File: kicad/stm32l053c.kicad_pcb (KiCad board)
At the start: 2 copper layers, 26.7 x 43.2 mm, 45 parts, among them J1 GND, J10 3V3, J11 I2C, J2 GND, J3 TX, J4 GND, J5 TEST_1P, J6 TEST_1P, J8 RX, P1 SWD, U1 AP2112, U2 STM32L053C8_LQFP48, U3 ADS1015, U4 UFL_SMA, U5 RFM92/95

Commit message: Start of layout
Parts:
- removed A0: A0, Pin_Headers:Pin_Header_Straight_1x01_Pitch2.54mm
- removed A1: A1, Pin_Headers:Pin_Header_Straight_1x01_Pitch2.54mm
- removed A2: A2, Pin_Headers:Pin_Header_Straight_1x01_Pitch2.54mm
- removed BT1: Battery, theapi:BatteryBoxAndPins
- removed C4: 10uF, Capacitors_SMD:C_0805_HandSoldering
- removed J10: 3V3, Pin_Headers:Pin_Header_Straight_1x01_Pitch2.54mm
- removed J11: I2C, Pin_Headers:Pin_Header_Straight_1x04_Pitch2.54mm
- removed J8: RX, Pin_Headers:Pin_Header_Straight_1x01_Pitch2.54mm
- removed PA6: A3, Pin_Headers:Pin_Header_Straight_1x01_Pitch2.54mm
- removed REF**: TheApiLogoTiny, theapi:TheApiLogoTiny
- removed REF**: TheApiLogo, theapi:TheApiLogoSmall
- removed SC1: Solar_Cells, Pin_Headers:Pin_Header_Straight_1x02_Pitch2.54mm
- added H1: MountingHole_Pad, MountingHole:MountingHole_3.2mm_M3_Pad, F.Cu at (83.8, 55.9)
- added H2: MountingHole_Pad, MountingHole:MountingHole_3.2mm_M3_Pad, F.Cu at (83.8, 104.1)
- added H3: MountingHole_Pad, MountingHole:MountingHole_3.2mm_M3_Pad, F.Cu at (166.4, 55.9)
- added H4: MountingHole_Pad, MountingHole:MountingHole_3.2mm_M3_Pad, F.Cu at (166.4, 104.1)
- added J7: BATTERY, Connector_JST:JST_XH_B02B-XH-A_1x02_P2.50mm_Vertical, F.Cu at (104.1, 101.6)
- added Q1: Q_NMOS_GSD, Package_TO_SOT_SMD:SOT-23_Handsoldering, F.Cu at (184.3, 53.3)
- added R12: 100K, Resistor_SMD:R_0805_2012Metric_Pad1.15x1.40mm_HandSolder, F.Cu at (175.0, 59.3)
- added R13: 1K, Resistor_SMD:R_0603_1608Metric_Pad1.05x0.95mm_HandSolder, F.Cu at (187.0, 55.8)
- added R14: 620K, Resistor_SMD:R_0805_2012Metric_Pad1.15x1.40mm_HandSolder, F.Cu at (200.5, 51.4)
- added R15: 100K, Resistor_SMD:R_0805_2012Metric_Pad1.15x1.40mm_HandSolder, F.Cu at (200.5, 53.4)
- added R16: 820, Resistor_SMD:R_0805_2012Metric_Pad1.15x1.40mm_HandSolder, F.Cu at (183.4, 56.0)
- added R17: 820, Resistor_SMD:R_0805_2012Metric_Pad1.15x1.40mm_HandSolder, F.Cu at (178.7, 59.3)
- added R18: 820, Resistor_SMD:R_0805_2012Metric_Pad1.15x1.40mm_HandSolder, F.Cu at (183.4, 58.0)
- added TH1: Thermistor_NTC, Connector_JST:JST_XH_B02B-XH-A_1x02_P2.50mm_Vertical, F.Cu at (104.1, 71.1)
- D2: value D_Schottky -> LED_CRGB; footprint theapi:D_SOD-323_HandSoldering -> Connector_JST:JST_XH_B04B-XH-A_1x04_P2.50mm_Vertical; moved to F.Cu
- J1: value GND -> Water_Level; footprint Pin_Headers:Pin_Header_Straight_1x01_Pitch2.54mm -> Connector_JST:JST_XH_B02B-XH-A_1x02_P2.50mm_Vertical
- J2: value GND -> Motion; footprint Pin_Headers:Pin_Header_Straight_1x01_Pitch2.54mm -> Connector_JST:JST_XH_B03B-XH-A_1x03_P2.50mm_Vertical
- J3: value TX -> Door; footprint Pin_Headers:Pin_Header_Straight_1x01_Pitch2.54mm -> Connector_JST:JST_XH_B02B-XH-A_1x02_P2.50mm_Vertical
- J4: value GND -> Door_Led; footprint Pin_Headers:Pin_Header_Straight_1x01_Pitch2.54mm -> Connector_JST:JST_XH_B02B-XH-A_1x02_P2.50mm_Vertical
- J5: value TEST_1P -> AIN3; footprint theapi:TestPoint -> Connector_PinHeader_2.54mm:PinHeader_1x02_P2.54mm_Vertical
- J6: value TEST_1P -> Pump; footprint theapi:TestPoint -> Connector_PinHeader_2.54mm:PinHeader_1x01_P2.54mm_Vertical
- R1, R7, R9: footprint Resistors_SMD:R_0805_HandSoldering -> Resistor_SMD:R_0805_2012Metric_Pad1.15x1.40mm_HandSolder
- R10, R2, R3, R4: footprint Resistors_SMD:R_0805_HandSoldering -> Resistor_SMD:R_0603_1608Metric_Pad1.05x0.95mm_HandSolder
- R11: value 4K7 -> 100K; footprint Resistors_SMD:R_0805_HandSoldering -> Resistor_SMD:R_0805_2012Metric_Pad1.15x1.40mm_HandSolder
- R5: value R_Shunt -> 0.01R; footprint theapi:SHUNT_1210_HandSoldering -> Connector_JST:JST_XH_B02B-XH-A_1x02_P2.50mm_Vertical; moved to F.Cu
- R6: value 300K -> 10K; footprint Resistors_SMD:R_0805_HandSoldering -> Resistor_SMD:R_0603_1608Metric_Pad1.05x0.95mm_HandSolder
- R8: value 100K -> 620K; footprint Resistors_SMD:R_0805_HandSoldering -> Resistor_SMD:R_0805_2012Metric_Pad1.15x1.40mm_HandSolder
- U1: value AP2112 -> MCP1703A-3302_SOT223; footprint TO_SOT_Packages_SMD:SOT-23-5_HandSoldering -> Package_TO_SOT_SMD:SOT-223-3_TabPin2; moved to F.Cu
- U3: footprint Housings_SSOP:TSSOP-10_3x3mm_Pitch0.5mm -> Package_SO:TSSOP-10_3x3mm_P0.5mm
- moved J4 77.5 mm to (83.8, 86.4), turned to 0 degrees
- moved J1 65.9 mm to (83.8, 71.1)
- moved J3 60.6 mm to (104.1, 86.4)
- moved D2 56.7 mm to (91.4, 55.9), turned to 0 degrees
- moved J2 44.4 mm to (116.8, 55.9)
- moved U1 18.5 mm to (124.5, 94.0), turned to 90 degrees
- moved R5 16.9 mm to (124.5, 71.1), turned to 0 degrees
- moved J5 9.78 mm to (165.1, 78.7)
- moved J6 3.94 mm to (160.0, 86.4)
- moved C8 1.63 mm to (138.2, 62.5)
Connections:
- net PA2 renamed USART2_TX
- C5 pad 1: /BATT -> +BATT
- D2 pad 1: /BATT -> Earth
- D2 pad 2: Net-(D2-Pad2) -> (no net)
- J1 pad 1: Earth -> SENSOR_PWR
- J2 pad 1: Earth -> +3V3
- J3 pad 1: USART1_TX -> +3V3
- J4 pad 1: Earth -> +3V3
- J5 pad 1: /PA4 -> Earth
- J6 pad 1: /PA3 -> PUMP
- R11 pad 1: +3V3 -> MOTION
- R11 pad 2: /1_WIRE -> Earth
- R5 pad 1: Net-(R5-Pad1) -> /AIN0
- R5 pad 2: /AIN0 -> /AIN1
- R6 pad 1: Net-(D2-Pad2) -> SENSOR_PWR
- R6 pad 2: /AIN2 -> WATER_TEMP
- R7 pad 1: /AIN2 -> WATER_LEVEL
- R8 pad 1: /BATT -> +BATT
- R8 pad 2: /AIN3 -> /AIN2
- R9 pad 1: /AIN3 -> /AIN2
- U1 pad 1: /BATT -> +BATT
- U1 pad 3: /BATT -> +3V3
- U2 pad 10: Net-(U2-Pad10) -> WATER_TEMP
- U2 pad 11: Net-(U2-Pad11) -> WATER_LEVEL
- U2 pad 13: /PA3 -> (no net)
- U2 pad 14: /PA4 -> SENSOR_PWR
- U2 pad 16: /1_WIRE -> DOOR_LED
- U2 pad 17: Net-(A2-Pad1) -> (no net)
- U2 pad 18: Net-(A1-Pad1) -> LED_RED
- U2 pad 19: Net-(A0-Pad1) -> LED_GREEN
- U2 pad 2: Net-(U2-Pad2) -> PUMP
- U2 pad 20: Net-(U2-Pad20) -> LED_BLUE
- U2 pad 21: DIO5 -> DIO0
- U2 pad 29: Net-(U2-Pad29) -> (no net)
- U2 pad 3: Net-(U2-Pad3) -> (no net)
- U2 pad 30: USART1_TX -> (no net)
- U2 pad 31: USART1_RX -> (no net)
- U2 pad 32: Net-(U2-Pad32) -> MOTION
- U2 pad 33: Net-(U2-Pad33) -> DOOR
- U2 pad 38: DIO3 -> (no net)
- U2 pad 39: DIO4 -> (no net)
- U2 pad 4: Net-(U2-Pad4) -> (no net)
- U2 pad 40: DIO0 -> (no net)
- U2 pad 41: DIO1 -> ADC_RDY
- U2 pad 45: DIO2 -> (no net)
- U2 pad 46: ADC_RDY -> (no net)
- U2 pad 5: Net-(U2-Pad5) -> (no net)
- U2 pad 6: Net-(U2-Pad6) -> (no net)
- U5 pad 11: DIO3 -> (no net)
- U5 pad 12: DIO4 -> (no net)
- U5 pad 15: DIO1 -> (no net)
- U5 pad 16: DIO2 -> (no net)
- U5 pad 7: DIO5 -> (no net)
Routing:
- net +3V3: track 172.7 -> 77.6 mm, vias 5 -> 4
- net Earth: track 210.2 -> 118.7 mm, vias 8 -> 6
- net /BATT: track 54.0 -> 0.00 mm, vias 1 -> 0
- net Net-(D2-Pad2): track 27.4 -> 0.00 mm
- net DIO5: track 26.8 -> 0.00 mm
- net USART1_RX: track 23.4 -> 0.00 mm, vias 1 -> 0
- net USART1_TX: track 23.4 -> 0.00 mm, vias 1 -> 0
- net +BATT: track 0.00 -> 20.9 mm, vias 0 -> 1
- net DIO3: track 19.4 -> 0.00 mm
- net DIO4: track 18.0 -> 0.00 mm
- net I2C1_SCL: track 32.6 -> 15.2 mm
- net /AIN0: track 15.4 -> 0.00 mm
- net I2C1_SDA: track 33.6 -> 18.5 mm
- net DIO0: track 15.5 -> 1.45 mm
- net DIO1: track 13.2 -> 0.00 mm
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- removed copper zone on B.Cu, net Earth
- removed copper zone on F.Cu, net Earth
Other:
- board size 26.7 x 43.2 mm -> 90 x 55 mm
- board text added: "BAT+"
- board text added: "BAT-"
- board text removed: "+"
- board text removed: "-"
- board text removed: "1WIRE"
- board text removed: "A0"
- board text removed: "A1"
- board text removed: "A2"
- board text removed: "BAT"
- board text removed: "SCL"
- board text removed: "SDA"
- board text removed: "SOL"

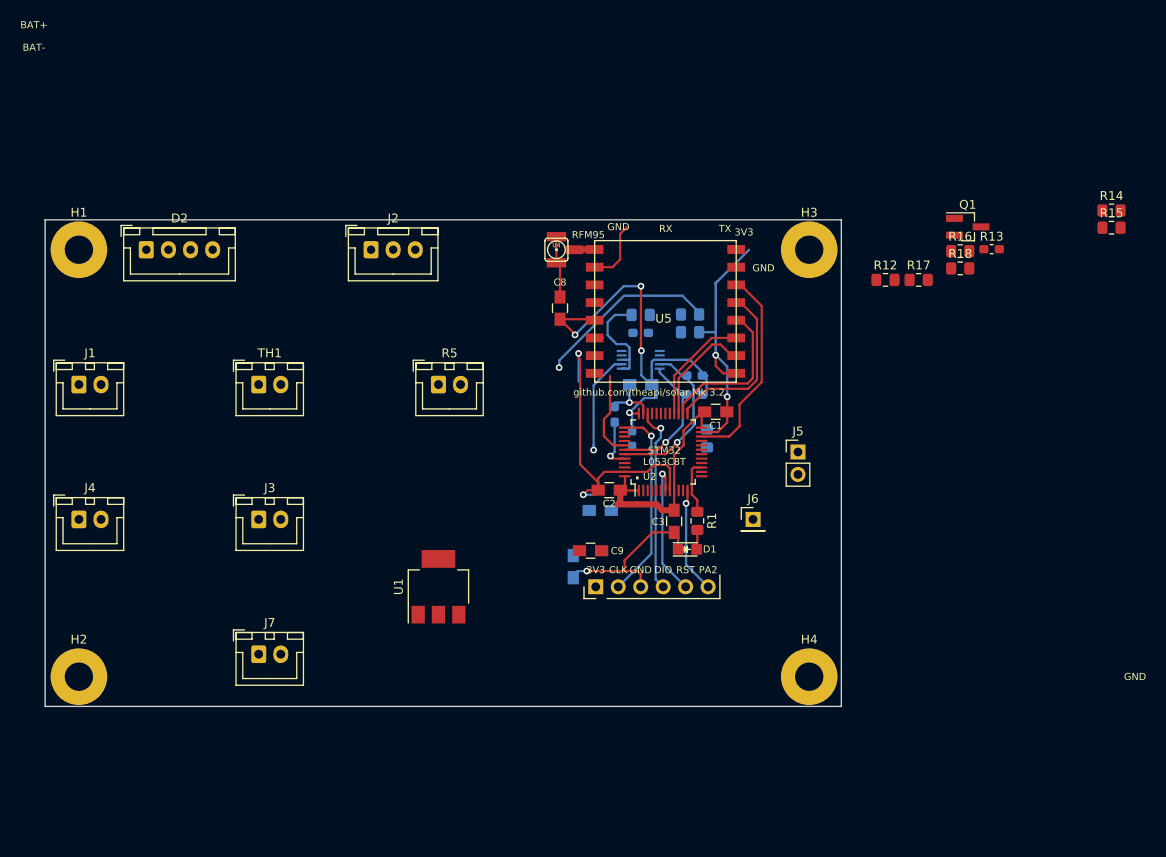
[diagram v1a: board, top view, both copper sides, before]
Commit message: Two voltage regulator layout
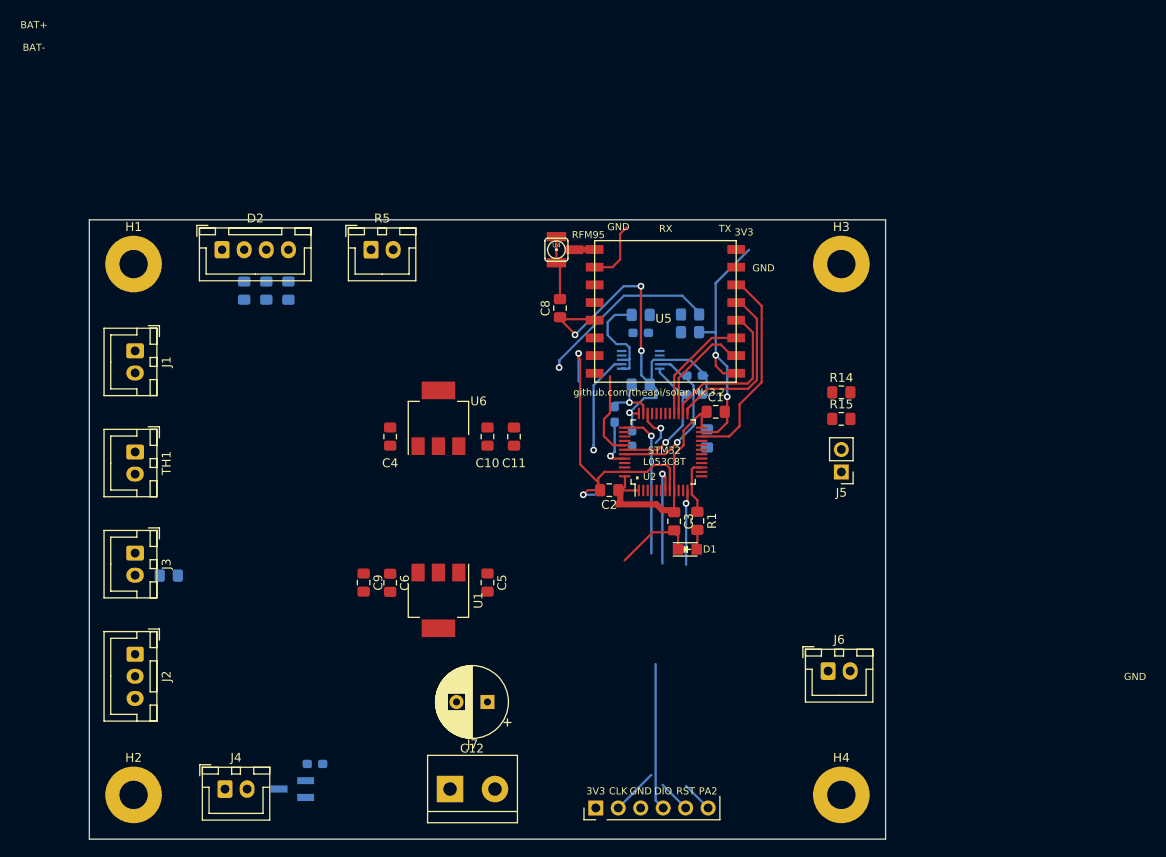
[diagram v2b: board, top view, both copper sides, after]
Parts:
- added C10: 1uf, Capacitor_SMD:C_0805_2012Metric_Pad1.15x1.40mm_HandSolder, F.Cu at (130.0, 77.0)
- added C11: 10uF, Capacitor_SMD:C_0805_2012Metric_Pad1.15x1.40mm_HandSolder, F.Cu at (133.0, 77.0)
- added C12: CP, Capacitor_THT:CP_Radial_D8.0mm_P3.50mm, F.Cu at (130.0, 107.0)
- added C4: 1uf, Capacitor_SMD:C_0805_2012Metric_Pad1.15x1.40mm_HandSolder, F.Cu at (119.0, 77.0)
- added U6: MCP1703A-3302_SOT223, Package_TO_SOT_SMD:SOT-223-3_TabPin2, F.Cu at (124.5, 74.9)
- C1, C2, C3, C7, C8, C9: footprint Capacitors_SMD:C_0805_HandSoldering -> Capacitor_SMD:C_0805_2012Metric_Pad1.15x1.40mm_HandSolder
- C5, C6: footprint Capacitors_SMD:C_0805_HandSoldering -> Capacitor_SMD:C_0805_2012Metric_Pad1.15x1.40mm_HandSolder; moved to F.Cu
- J6: footprint Connector_PinHeader_2.54mm:PinHeader_1x01_P2.54mm_Vertical -> Connector_JST:JST_XH_B02B-XH-A_1x02_P2.50mm_Vertical
- J7: footprint Connector_JST:JST_XH_B02B-XH-A_1x02_P2.50mm_Vertical -> TerminalBlock:TerminalBlock_bornier-2_P5.08mm
- Q1, R12, R13, R16, R17, R18: moved to B.Cu
- U1: value MCP1703A-3302_SOT223 -> MCP1703A-5002_SOT223
- moved Q1 99.3 mm to (108.0, 116.8), turned to 180 degrees
- moved R13 96.1 mm to (110.5, 114.0), turned to 180 degrees
- moved R12 87.6 mm to (94.0, 92.7)
- moved R16 81.1 mm to (102.5, 60.5), turned to 90 degrees
- moved R18 76.0 mm to (107.5, 60.5), turned to 90 degrees
- moved R17 73.7 mm to (105.0, 60.5), turned to 90 degrees
- moved J2 52.9 mm to (90.2, 101.6), turned to 270 degrees
- moved R15 37.4 mm to (170.0, 75.0)
- moved R14 36.8 mm to (170.0, 72.0)
- moved J4 34.7 mm to (100.3, 116.8)
- moved J7 26.5 mm to (125.8, 116.8)
- moved C9 25.9 mm to (116.0, 93.5), turned to 270 degrees
- moved P1 25.0 mm to (142.2, 119.0)
- moved C6 20.8 mm to (119.0, 93.5)
- moved J6 19.1 mm to (168.5, 103.5)
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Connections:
- C6 pad 1: +3V3 -> +5V
- C9 pad 1: +3V3 -> +5V
- D2 pad 2: (no net) -> Net-(D2-Pad2)
- D2 pad 3: (no net) -> Net-(D2-Pad3)
- D2 pad 4: (no net) -> Net-(D2-Pad4)
- J2 pad 1: +3V3 -> +5V
- J4 pad 1: +3V3 -> +5V
- J7 pad 1: +BATT -> Earth
- J7 pad 2: Earth -> +BATT
- R16 pad 2: (no net) -> Net-(D2-Pad2)
- R17 pad 2: (no net) -> Net-(D2-Pad3)
- R18 pad 2: (no net) -> Net-(D2-Pad4)
- U1 pad 3: +3V3 -> +5V
- U2 pad 13: (no net) -> USART2_RX
- U2 pad 17: (no net) -> Net-(U2-Pad17)
- U2 pad 29: (no net) -> Net-(U2-Pad29)
- U2 pad 3: (no net) -> Net-(U2-Pad3)
- U2 pad 30: (no net) -> Net-(U2-Pad30)
- U2 pad 31: (no net) -> Net-(U2-Pad31)
- U2 pad 38: (no net) -> Net-(U2-Pad38)
- U2 pad 39: (no net) -> Net-(U2-Pad39)
- U2 pad 4: (no net) -> Net-(U2-Pad4)
- U2 pad 40: (no net) -> Net-(U2-Pad40)
- U2 pad 45: (no net) -> Net-(U2-Pad45)
- U2 pad 46: (no net) -> Net-(U2-Pad46)
- U2 pad 5: (no net) -> Net-(U2-Pad5)
- U2 pad 6: (no net) -> Net-(U2-Pad6)
- U5 pad 11: (no net) -> Net-(U5-Pad11)
- U5 pad 12: (no net) -> Net-(U5-Pad12)
- U5 pad 15: (no net) -> Net-(U5-Pad15)
- U5 pad 16: (no net) -> Net-(U5-Pad16)
- U5 pad 7: (no net) -> Net-(U5-Pad7)
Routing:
- net Earth: track 118.7 -> 108.1 mm, vias 6 -> 5
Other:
- board size 90 x 55 mm -> 90 x 70 mm

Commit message: Protection
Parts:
- added D3: 3V6, Diode_THT:D_T-1_P5.08mm_Horizontal, F.Cu at (130.0, 83.6)
- added F1: Polyfuse, Resistor_SMD:R_1812_4532Metric_Pad1.30x3.40mm_HandSolder, F.Cu at (130.8, 104.0)
- added Q2: Q_PMOS_GSD, Package_TO_SOT_SMD:SOT-23_Handsoldering, F.Cu at (129.8, 109.6)
- added R19: 1K, Resistor_SMD:R_0603_1608Metric_Pad1.05x0.95mm_HandSolder, B.Cu at (119.2, 60.2)
- added R20: 1K, Resistor_SMD:R_0603_1608Metric_Pad1.05x0.95mm_HandSolder, B.Cu at (116.8, 60.2)
- added R21: 1K, Resistor_SMD:R_0603_1608Metric_Pad1.05x0.95mm_HandSolder, F.Cu at (136.0, 77.0)
- moved C12 8.81 mm to (121.2, 106.6)
- moved J7 2.77 mm to (123.0, 116.8)
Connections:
- C12 pad 1: +BATT -> Net-(C12-Pad1)
- C12 pad 2: Earth -> Net-(C12-Pad2)
- C5 pad 1: +BATT -> Net-(C12-Pad1)
- C5 pad 2: Earth -> Net-(C12-Pad2)
- R5 pad 1: /AIN0 -> Net-(R20-Pad2)
- R5 pad 2: /AIN1 -> Net-(R19-Pad2)
- R8 pad 1: +BATT -> /BATT
- U1 pad 1: +BATT -> Net-(C12-Pad1)
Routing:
- net SWDIO: track 21.2 -> 46.5 mm
- net NRST: track 15.8 -> 40.8 mm
- net USART2_TX: track 12.0 -> 37.0 mm
- net SWCLK: track 22.0 -> 47.0 mm
- net /BATT: track 0.00 -> 20.9 mm, vias 0 -> 1
- net +BATT: track 20.9 -> 0.00 mm, vias 1 -> 0
- net Earth: track 108.1 -> 90.0 mm
- net ADC_RDY: track 21.3 -> 13.2 mm
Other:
- board text added: "5V"

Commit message: Solder mask for the ADS1015
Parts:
- U3: footprint Package_SO:TSSOP-10_3x3mm_P0.5mm -> theapi:TSSOP-10_3x3mm_P0.5mm
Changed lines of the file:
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@@
-    )
-  )
-  (module Package_SO:TSSOP-10_3x3mm_P0.5mm (layer B.Cu)
-    (at 147.32 68.326)
-    (descr "TSSOP10: plastic thin shrink small outline package; 10 leads; body width 3 mm; (see NXP SSOP-TSSOP-VSO-REFLOW.pdf and sot552-1_po.pdf)")
-    (tags "SSOP 0.5")
-    (attr smd)
-    (fp_text reference U3 (at 0 2.55) (layer B.SilkS)
-      (effects (font (size 1 1) (thickness 0.15)) (justify mirror))
-    )
-    (fp_text value ADS1015 (at 0 -2.55) (layer B.Fab)
-      (effects (font (size 1 1) (thickness 0.15)) (justify mirror))
-    )
-    (fp_line (start -0.5 1.5) (end 1.5 1.5) (layer B.Fab) (width 0.15))
-    (fp_line (start 1.5 1.5) (end 1.5 -1.5) (layer B.Fab) (width 0.15))
-    (fp_line (start 1.5 -1.5) (end -1.5 -1.5) (layer B.Fab) (width 0.15))
-    (fp_line (start -1.5 -1.5) (end -1.5 0.5) (layer B.Fab) (width 0.15))
-    (fp_line (start -1.5 0.5) (end -0.5 1.5) (layer B.Fab) (width 0.15))
-    (fp_line (start -2.95 1.8) (end -2.95 -1.8) (layer B.CrtYd) (width 0.05))
-    (fp_line (start 2.95 1.8) (end 2.95 -1.8) (layer B.CrtYd) (width 0.05))
-    (fp_line (start -2.95 1.8) (end 2.95 1.8) (layer B.CrtYd) (width 0.05))
-    (fp_line (start -2.95 -1.8) (end 2.95 -1.8) (layer B.CrtYd) (width 0.05))
-    (fp_line (start -1.625 1.625) (end -1.625 1.45) (layer B.SilkS) (width 0.15))
-    (fp_line (start 1.625 1.625) (end 1.625 1.35) (layer B.SilkS) (width 0.15))
-    (fp_line (start 1.625 -1.625) (end 1.625 -1.35) (layer B.SilkS) (width 0.15))
-    (fp_line (start -1.625 -1.625) (end -1.625 -1.35) (layer B.SilkS) (width 0.15))
-    (fp_line (start -1.625 1.625) (end 1.625 1.625) (layer B.SilkS) (width 0.15))
-    (fp_line (start -1.625 -1.625) (end 1.625 -1.625) (layer B.SilkS) (width 0.15))
-    (fp_line (start -1.625 1.45) (end -2.7 1.45) (layer B.SilkS) (width 0.15))
-    (fp_text user %R (at 0 0) (layer B.Fab)
-      (effects (font (size 0.6 0.6) (thickness 0.15)) (justify mirror))
-    )
-    (pad 1 smd rect (at -2.15 1) (size 1.1 0.25) (layers B.Cu B.Paste B.Mask)
-      (net 1 Earth))
-    (pad 2 smd rect (at -2.15 0.5) (size 1.1 0.25) (layers B.Cu B.Paste B.Mask)
-      (net 9 ADC_RDY))
-    (pad 3 smd rect (at -2.15 0) (size 1.1 0.25) (layers B.Cu B.Paste B.Mask)
-      (net 1 Earth))
-    (pad 4 smd rect (at -2.15 -0.5) (size 1.1 0.25) (layers B.Cu B.Paste B.Mask)
-      (net 19 /AIN0))
-    (pad 5 smd rect (at -2.15 -1) (size 1.1 0.25) (layers B.Cu B.Paste B.Mask)
-      (net 21 /AIN1))
-    (pad 6 smd rect (at 2.15 -1) (size 1.1 0.25) (layers B.Cu B.Paste B.Mask)
-      (net 13 /AIN2))
-    (pad 7 smd rect (at 2.15 -0.5) (size 1.1 0.25) (layers B.Cu B.Paste B.Mask)
-      (net 20 /AIN3))
-    (pad 8 smd rect (at 2.15 0) (size 1.1 0.25) (layers B.Cu B.Paste B.Mask)
-      (net 6 +3V3))
-    (pad 9 smd rect (at 2.15 0.5) (size 1.1 0.25) (layers B.Cu B.Paste B.Mask)
-      (net 7 I2C1_SDA))
-    (pad 10 smd rect (at 2.15 1) (size 1.1 0.25) (layers B.Cu B.Paste B.Mask)
-      (net 8 I2C1_SCL))
-    (model ${KISYS3DMOD}/Package_SO.3dshapes/TSSOP-10_3x3mm_P0.5mm.wrl
-      (at (xyz 0 0 0))
-      (scale (xyz 1 1 1))
-      (rotate (xyz 0 0 0))
     )
   )
@@
       (at (xyz 0 0 0))
       (scale (xyz 1 1 1))
+      (rotate (xyz 0 0 0))
+    )
+  )
+  (module theapi:TSSOP-10_3x3mm_P0.5mm (layer B.Cu)
+    (at 147.32 68.326)
+    (descr "TSSOP10: plastic thin shrink small outline package; 10 leads; body width 3 mm; (see NXP SSOP-TSSOP-VSO-REFLOW.pdf and sot552-1_po.pdf)")
+    (tags "SSOP 0.5")
+    (solder_mask_margin 0.07)
+    (attr smd)
+    (fp_text reference U3 (at 0 2.55) (layer B.SilkS)
+      (effects (font (size 1 1) (thickness 0.15)) (justify mirror))
+    )
+    (fp_text value ADS1015 (at 0 -2.55) (layer B.Fab)
+      (effects (font (size 1 1) (thickness 0.15)) (justify mirror))
+    )
+    (fp_line (start -0.5 1.5) (end 1.5 1.5) (layer B.Fab) (width 0.15))
+    (fp_line (start 1.5 1.5) (end 1.5 -1.5) (layer B.Fab) (width 0.15))
+    (fp_line (start 1.5 -1.5) (end -1.5 -1.5) (layer B.Fab) (width 0.15))
+    (fp_line (start -1.5 -1.5) (end -1.5 0.5) (layer B.Fab) (width 0.15))
+    (fp_line (start -1.5 0.5) (end -0.5 1.5) (layer B.Fab) (width 0.15))
+    (fp_line (start -2.95 1.8) (end -2.95 -1.8) (layer B.CrtYd) (width 0.05))
+    (fp_line (start 2.95 1.8) (end 2.95 -1.8) (layer B.CrtYd) (width 0.05))
+    (fp_line (start -2.95 1.8) (end 2.95 1.8) (layer B.CrtYd) (width 0.05))
+    (fp_line (start -2.95 -1.8) (end 2.95 -1.8) (layer B.CrtYd) (width 0.05))
+    (fp_line (start -1.625 1.625) (end -1.625 1.45) (layer B.SilkS) (width 0.15))
+    (fp_line (start 1.625 1.625) (end 1.625 1.35) (layer B.SilkS) (width 0.15))
+    (fp_line (start 1.625 -1.625) (end 1.625 -1.35) (layer B.SilkS) (width 0.15))
+    (fp_line (start -1.625 -1.625) (end -1.625 -1.35) (layer B.SilkS) (width 0.15))
+    (fp_line (start -1.625 1.625) (end 1.625 1.625) (layer B.SilkS) (width 0.15))
+    (fp_line (start -1.625 -1.625) (end 1.625 -1.625) (layer B.SilkS) (width 0.15))
+    (fp_line (start -1.625 1.45) (end -2.7 1.45) (layer B.SilkS) (width 0.15))
+    (fp_text user %R (at 0 0) (layer B.Fab)
+      (effects (font (size 0.6 0.6) (thickness 0.15)) (justify mirror))
+    )
+    (pad 1 smd rect (at -2.15 1) (size 1.1 0.25) (layers B.Cu B.Paste B.Mask)
+      (net 1 Earth))
+    (pad 2 smd rect (at -2.15 0.5) (size 1.1 0.25) (layers B.Cu B.Paste B.Mask)
+      (net 9 ADC_RDY))
+    (pad 3 smd rect (at -2.15 0) (size 1.1 0.25) (layers B.Cu B.Paste B.Mask)
+      (net 1 Earth))
+    (pad 4 smd rect (at -2.15 -0.5) (size 1.1 0.25) (layers B.Cu B.Paste B.Mask)
+      (net 19 /AIN0))
+    (pad 5 smd rect (at -2.15 -1) (size 1.1 0.25) (layers B.Cu B.Paste B.Mask)
+      (net 21 /AIN1))
+    (pad 6 smd rect (at 2.15 -1) (size 1.1 0.25) (layers B.Cu B.Paste B.Mask)
+      (net 13 /AIN2))
+    (pad 7 smd rect (at 2.15 -0.5) (size 1.1 0.25) (layers B.Cu B.Paste B.Mask)
+      (net 20 /AIN3))
+    (pad 8 smd rect (at 2.15 0) (size 1.1 0.25) (layers B.Cu B.Paste B.Mask)
+      (net 6 +3V3))
+    (pad 9 smd rect (at 2.15 0.5) (size 1.1 0.25) (layers B.Cu B.Paste B.Mask)
+      (net 7 I2C1_SDA))
+    (pad 10 smd rect (at 2.15 1) (size 1.1 0.25) (layers B.Cu B.Paste B.Mask)
+      (net 8 I2C1_SCL))
+    (model ${KISYS3DMOD}/Package_SO.3dshapes/TSSOP-10_3x3mm_P0.5mm.wrl
+      (at (xyz 0 0 0))
+      (scale (xyz 1 1 1))
